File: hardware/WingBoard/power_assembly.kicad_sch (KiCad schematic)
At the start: 16 parts

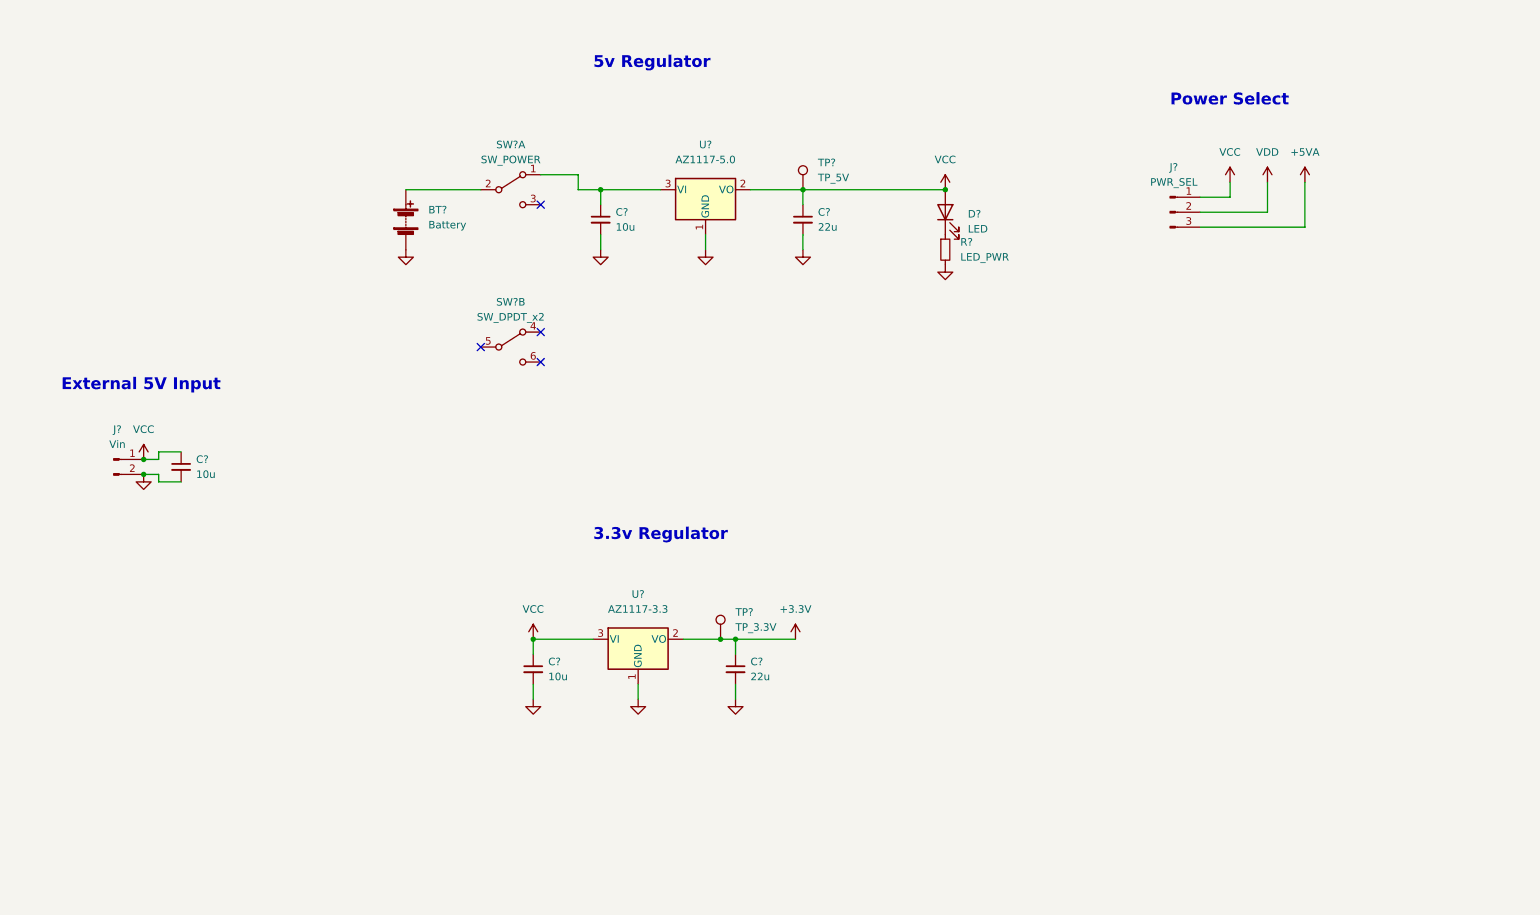
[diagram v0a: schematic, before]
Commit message: Hardware update: status LEDs, DIP switches, & test points.
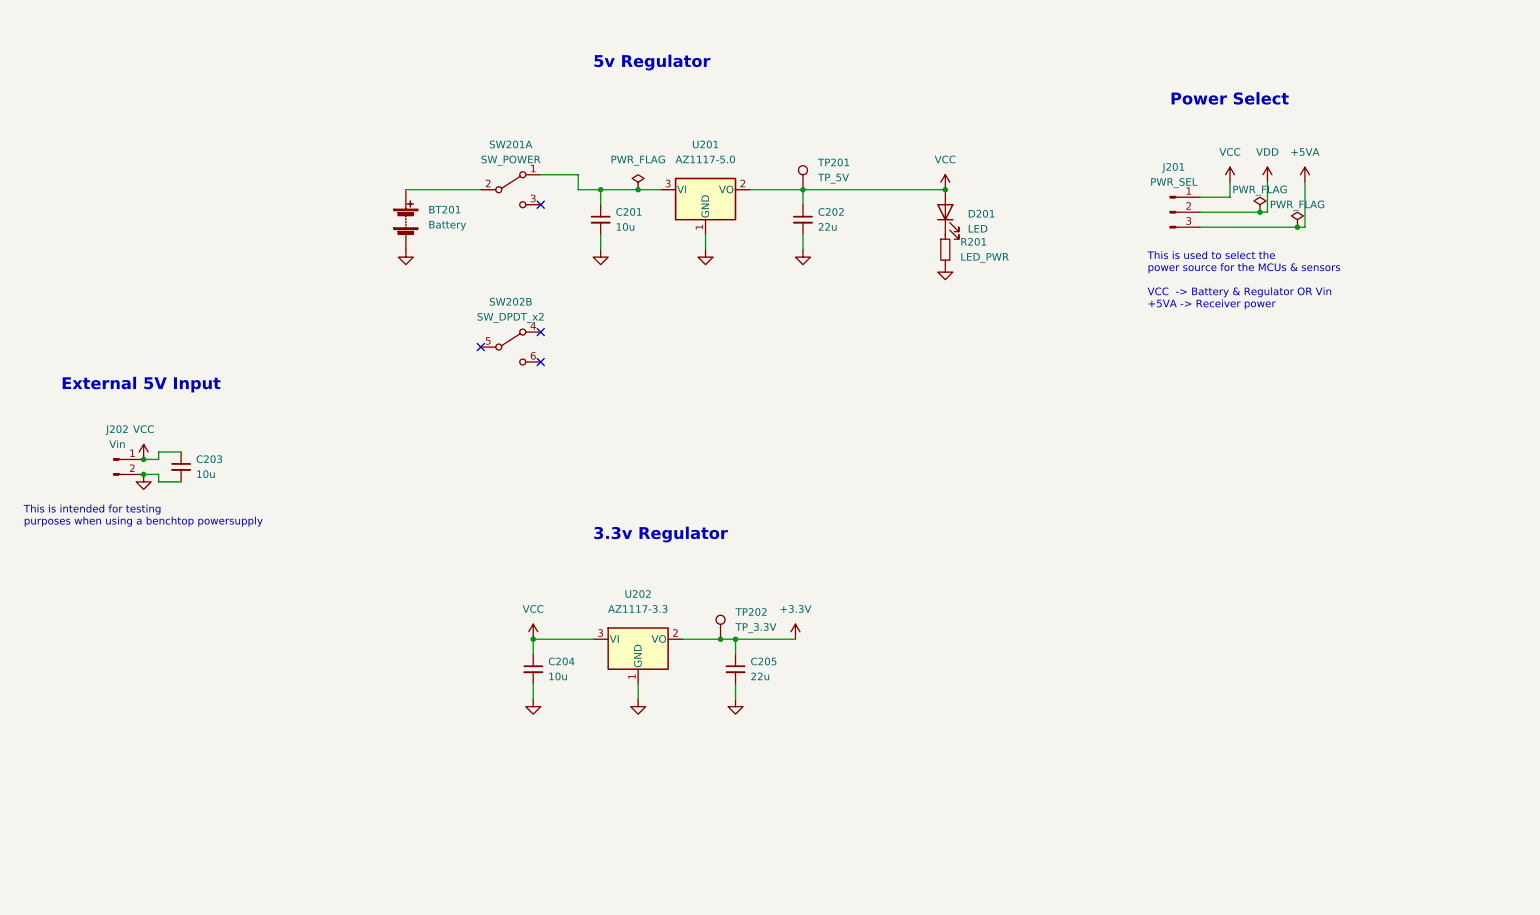
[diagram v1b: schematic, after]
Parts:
- gave numbers to parts that had none: 16
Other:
- note added: "This is intended for testing purposes when using a benchtop powersupply"
- note added: "This is used to select the power source for the MCUs & sensors VCC -> Battery & Regulator OR Vin +5VA -> Receiver power"

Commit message: Minor hardware design updates and assigned PCB footprints
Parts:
- removed SW202: SW_DPDT_x2, symbol Switch:SW_DPDT_x2
- added D202: 3V, LED_SMD:LED_0805_2012Metric_Pad1.15x1.40mm_HandSolder, symbol Device:LED
- added R202: LED_PWR, Resistor_SMD:R_0805_2012Metric_Pad1.20x1.40mm_HandSolder, symbol Device:R_Small
- BT201: footprint (none) -> Connector_AMASS:AMASS_XT30U-M_1x02_P5.0mm_Vertical
- C201, C202, C203, C204, C205: footprint (none) -> Capacitor_SMD:C_0805_2012Metric_Pad1.18x1.45mm_HandSolder
- D201: value LED -> 5V; footprint (none) -> LED_SMD:LED_0805_2012Metric_Pad1.15x1.40mm_HandSolder
- J201: footprint (none) -> Connector_PinHeader_2.54mm:PinHeader_1x03_P2.54mm_Vertical
- J202: footprint (none) -> Connector_PinHeader_2.54mm:PinHeader_1x02_P2.54mm_Vertical
- R201: footprint (none) -> Resistor_SMD:R_0805_2012Metric_Pad1.20x1.40mm_HandSolder
- SW201: footprint (none) -> Button_Switch_SMD:SW_DPDT_MSS22D18_6pin_bje
- TP201, TP202: footprint (none) -> TestPoint:TestPoint_Pad_D1.5mm
- U201: footprint (none) -> ICs:AZ1117CH-5.0TRG1
- U202: footprint (none) -> ICs:AZ1117CR-3.3TRG1
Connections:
- net +3V3: now also D202.2 (A)
- net GND: now also R202.2
- new net: D202.1 (K), R202.1
- no-connect marks 4 -> 1

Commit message: PCB rough layout done.
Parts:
- C201, C202, C204, C205: footprint Capacitor_SMD:C_0805_2012Metric_Pad1.18x1.45mm_HandSolder -> Capacitor_THT:CP_Radial_D4.0mm_P1.50mm
- U201: footprint ICs:AZ1117CH-5.0TRG1 -> Proj ICs:AZ1117CH-5.0TRG1
- U202: footprint ICs:AZ1117CR-3.3TRG1 -> Proj ICs:AZ1117CR-3.3TRG1
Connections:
- net VCC: no longer C204.1, U202.3 (VI)
- net VDD: now also C204.1, U202.3 (VI)
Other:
- note added: "This is intended for testing purposes when using a benchtop powersupply. Non-regulated: Must be ~5 volts."
- note added: "This is used to select the power source for the MCUs & sensors VCC -> Battery (regulated to 5V) OR Vin (non-regulated) +5VA -> Power from RC receiver"
- note removed: "This is intended for testing purposes when using a benchtop powersupply"
- note removed: "This is used to select the power source for the MCUs & sensors VCC -> Battery & Regulator OR Vin +5VA -> Receiver power"
- moved on the sheet: C204, C205, D202, J201, R202, TP202, U202

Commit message: Hardware layout v0.1 complete.
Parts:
- removed D202: 3V, LED_SMD:LED_0805_2012Metric_Pad1.15x1.40mm_HandSolder, symbol Device:LED
- removed R202: LED_PWR, Resistor_SMD:R_0805_2012Metric_Pad1.20x1.40mm_HandSolder, symbol Device:R_Small
- removed TP201: TP_5V, TestPoint:TestPoint_Pad_D1.5mm, symbol Connector:TestPoint
- removed TP202: TP_3.3V, TestPoint:TestPoint_Pad_D1.5mm, symbol Connector:TestPoint
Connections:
- net +5VA: now also C204.1
- net VCC: no longer D201.2 (A)
- net VDD: now also D201.2 (A); no longer C204.1
- net 5V_REG_IN: now reaches C201.1, SW201.1 (A), U201.3 (VI)
- net BAT+: now reaches BT201.1 (+), SW201.2 (B)
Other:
- note added: "Power LED"
- moved on the sheet: BT201, C201, C202, C203, C205, D201, J201, J202, R201, SW201A, U201, U202
